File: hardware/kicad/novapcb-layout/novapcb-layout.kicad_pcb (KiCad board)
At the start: 4 copper layers, 36 x 36 mm, 70 parts, among them J1 USB-C_2.0, J10 CRSF_4P, J11 ESC_solder_pad, J12 ESC_solder_pad, J13 ESC_solder_pad, J14 ESC_solder_pad, J15 ESC_solder_pad, J16 ESC_solder_pad, J17 ESC_solder_pad, J18 ESC_solder_pad, J2 microSD_DM3AT, J3 TELEM_6P, J4 MAUCH_6P, J5 GPS_MAG_10P, J9 SWD_10P, U1 STM32H743VITx, U2 AP2112K-3.3, U3 ICM-42688-P, U4 DPS310, U5 USBLC6-2P6, Y1 8MHz

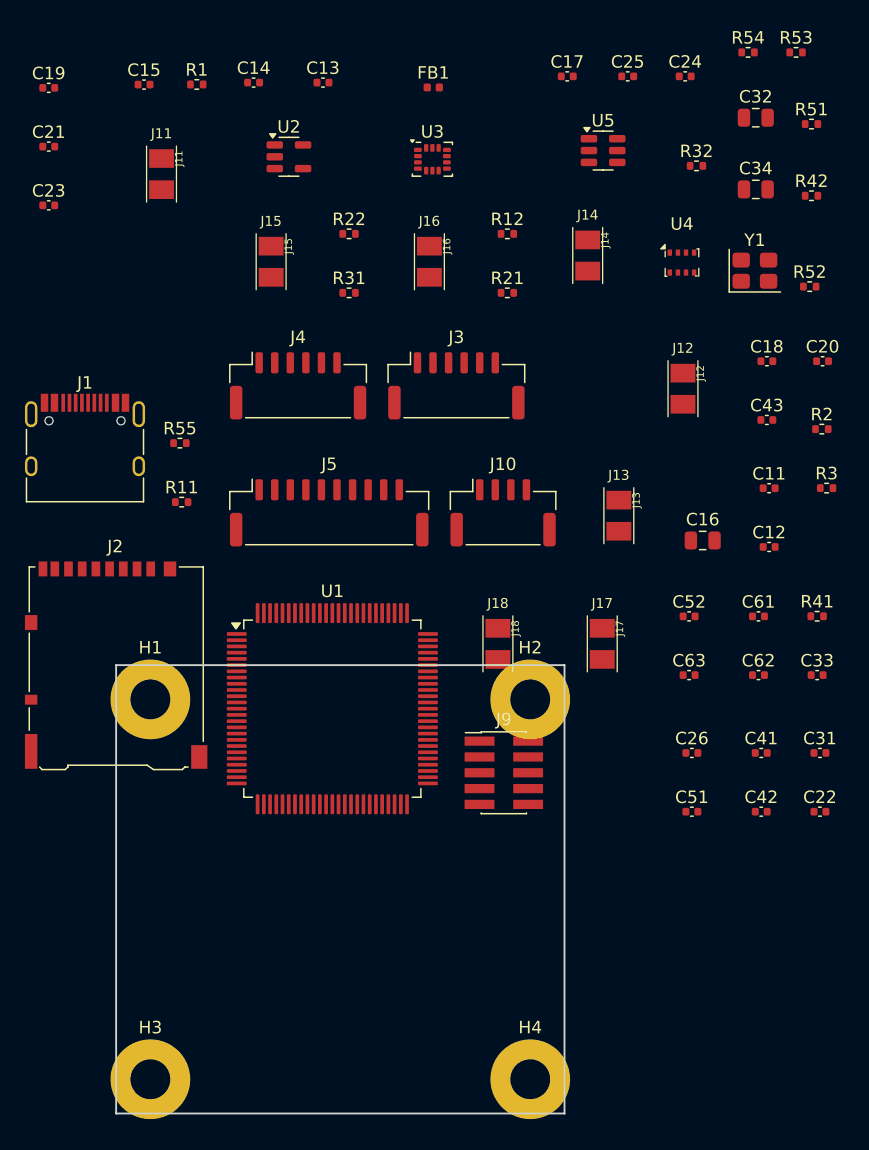
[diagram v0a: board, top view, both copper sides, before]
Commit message: Phase 4b: component placement (routing-aware first-pass) (#43)
* Phase 4b: component placement (routing-aware first-pass)

70 components placed on the 36×36 board with per-component-group
routing-aware reasoning. Master 09:00 cross-review emphasis: "4b is the
highest-leverage Phase 4 sub-phase; treat as design, not mechanics."

## Per-group placement reasoning (summary)

- MCU (U1) centered at (18,19) — geometric center for 4-edge routing
  reach; +1mm N to leave Y=0..11 for ESC pads bottom row
- Crystal (Y1) hard against MCU east (HSE pins per STM32H743V)
- LDO (U2 AP2112K) SW at (6,9) — near 5V input from Mauch path
- IMU (U3 ICM-42688-P) west of MCU at (8,22) — board-center-Y for
  rotational sensing; off-axis from LDO heat + ESC switching noise
- Baro (U4 DPS310) N of MCU at (22,28) — close to I²C2 pins
- GPS+mag (J5 JST-GH 10P) left edge
- USB-C (J1) top center — short diff pair to MCU PA11/PA12;
  USBLC6 ESD (U5) west of J1 body to clear J1 courtyard
- CRSF (J10), Telem (J3), Mauch (J4) right edge top/mid/bottom
- microSD (J2) FLIPPED TO B.CU — resolves Phase 2.5 tight-spot #1
  (microSD vs IMU vertical-clearance collision)
- 8× ESC solder pads (J11-J18) bottom edge single row, 3.0mm pitch
- SWD (J9) B.Cu under MCU center for pogo-pin programming
- 4× M3 mounting (H1-H4) corners at exact 30.5 c-to-c
- 50+ passives positioned per-IC: MCU decoupling around 4 sides ≥2.5mm
  from body edge; ADC filter near MCU PC0/PC1 (PHASE3_AUDIT §B #5);
  SDMMC pullups between J2 and MCU; CC pulldowns near J1

## Phase 2.5 sketch refinements

- J6 CAN REMOVED (phase3exit-can deliberate v1-omit) — frees right edge
- J2 microSD FLIPPED to B.Cu — resolves the IMU-vs-microSD collision
- 8× solder pads replace 2× JST-SH 4P (Phase 4a footprint swap)
- Other connectors refined for cleaner right-edge separation

## DRC honesty

`kicad-cli pcb drc --severity-error`:
- 4a baseline: 16 courtyard-overlap from kinet2pcb grid
- 4b after placement: 87 violations, 0 unconnected

Breakdown:
- 4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
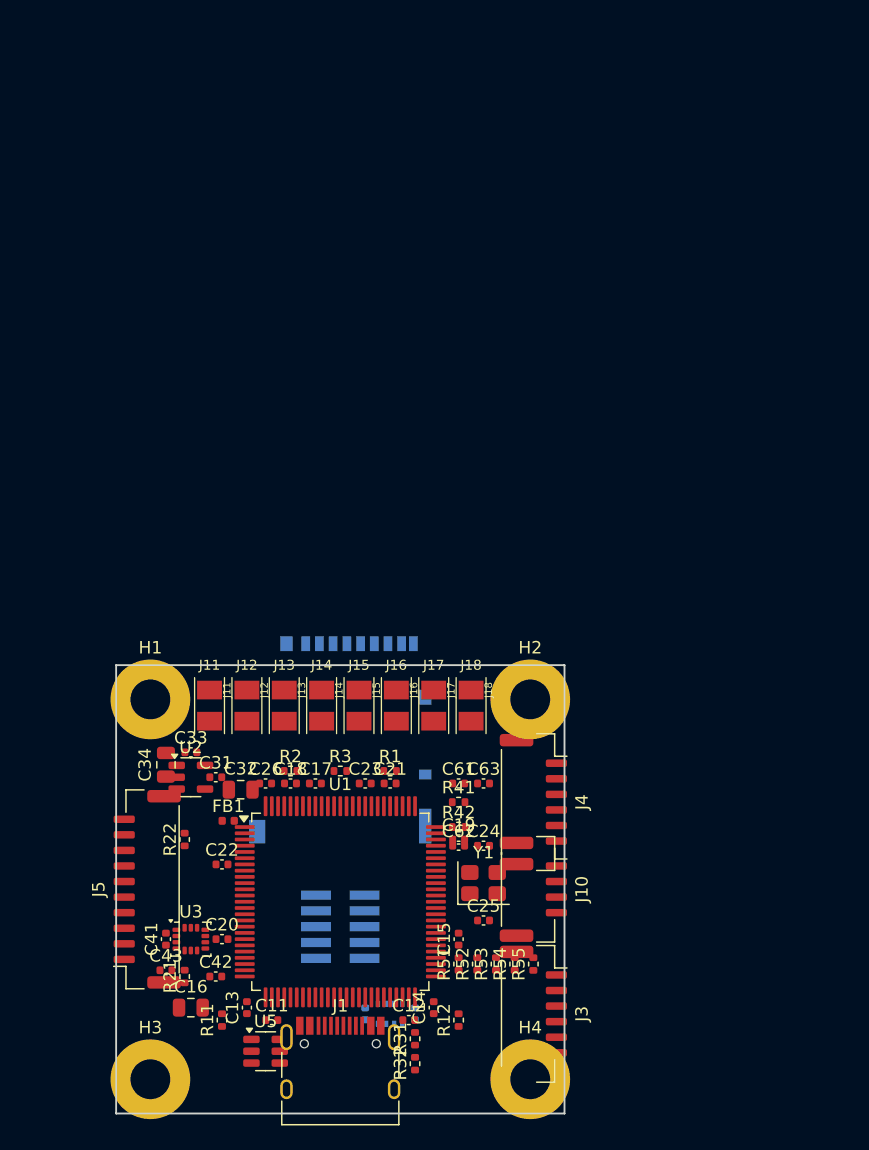
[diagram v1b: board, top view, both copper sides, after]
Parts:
- C51, C52, J2, J9, U4: moved to B.Cu
- moved U5 77.2 mm to (12.0, 31.0)
- moved R53 77.1 mm to (30.5, 24.0), turned to 90 degrees
- moved C14 75.7 mm to (25.5, 27.5), turned to 90 degrees
- moved R54 75.6 mm to (32.0, 24.0), turned to 90 degrees
- moved R32 75.5 mm to (24.0, 32.0), turned to 90 degrees
- moved C13 74.5 mm to (10.5, 27.5), turned to 90 degrees
- moved R51 73.2 mm to (27.5, 24.0), turned to 90 degrees
- moved C15 73.1 mm to (27.5, 22.0), turned to 90 degrees
- moved C25 68.8 mm to (29.5, 20.5)
- moved C19 68.7 mm to (27.5, 14.0)
- moved C32 68.0 mm to (10.0, 10.0)
- moved C20 66.9 mm to (8.50, 22.0)
- moved C34 66.2 mm to (4.00, 8.00), turned to 90 degrees
- moved U3 65.6 mm to (6.00, 22.0)
- moved C43 65.4 mm to (4.00, 24.5)
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
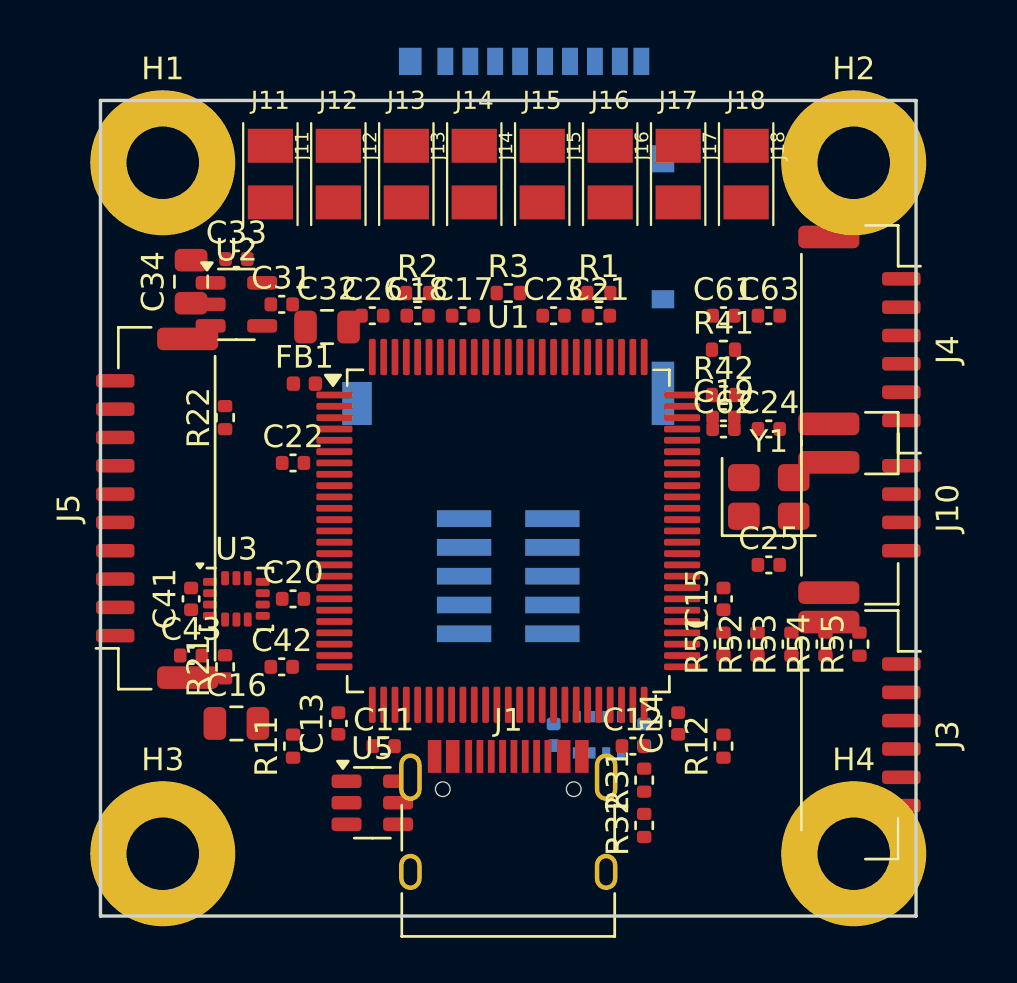
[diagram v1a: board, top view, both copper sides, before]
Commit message: Phase 4c: copper plane pour (Rule 13 stop at 4c.6 — 5 shorts persist)
Plane pour implemented per master's iter-#3 P0 pre-conditions. 4c.6
DRC re-check triggers Rule 13 stop per master's 4b adjudication
("If any do NOT resolve, that's a Rule 13 stop").

## What got done

7 copper zones added + persisted in .kicad_pcb:
- In1.Cu  GND   solid pour (full board minus 0.2mm edge inset)
- In2.Cu  +3V3  dominant (full board, low priority)
- In2.Cu  +5V   top band (Y>22): USB-C + N half of right edge
- In2.Cu  +5V   LDO strip (SW corner): U2 input
- In2.Cu  VBAT  small rect (S of MCU + J4 Mauch)
- In2.Cu  +3V3A tiny zone (MCU VDDA via FB1)
- B.Cu    GND   fill in unused areas (signal+GND-fill per fork)

DRC result:
- unconnected_items: 193 → 0 ✓ (planes connecting pads correctly)
- shorting_items: 5 → 5 (UNCHANGED — F.Cu pad-pad physical overlaps,
  plane pour on inner layers doesn't move pads)
- clearance: 13 (unchanged from 4b-rev)
- total: 18 (same as 4b-rev; planes didn't add violations but didn't
  resolve the shorts either)

## Rule 13 stop — 5 unresolved shorting_items

The 4b assumption "cap-GND shorts auto-resolve at 4c plane pour" was
WRONG. All 5 persist because they're F.Cu pad-pad physical overlaps:

1. U2 LDO pad-2 [GND] @ (4.86,9.00) ↔ C34 pad-1 [+3V3] @ (4.00,8.95)
2. U5 pad-5 [+5V] @ (13.14,31.00) ↔ J1 USB-C PTH shield [GND] @ (13.68,29.87)
3. U5 pad-6 [USB_DP] @ (13.14,30.05) ↔ J1 shield same position
4. C62 [BATT_CURRENT_SENS] @ (27.02,14.50) ↔ C19 [+3V3A] @ (27.02,14.00)
5. C26 [NRST] @ (11.52,9.50) ↔ C32 [GND] @ (10.95,10.00)

All 5 fixable by ~1-2mm targeted nudges (worker did NOT apply — 4c
scope is planes, not placement). Master adjudicates options A/B/C in
phase-4c-planes.yaml escalation_log #1; worker recommends B (4b-rev3
targeted nudges on the 5 specific F.Cu pad collisions).

## Two pcbnew Python binding bugs discovered + worked around

Both logged in KICAD9_NOTES.md (cross-machine source of truth):

1. **ZONE.SetOutline(SHAPE_POLY_SET) holds outl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
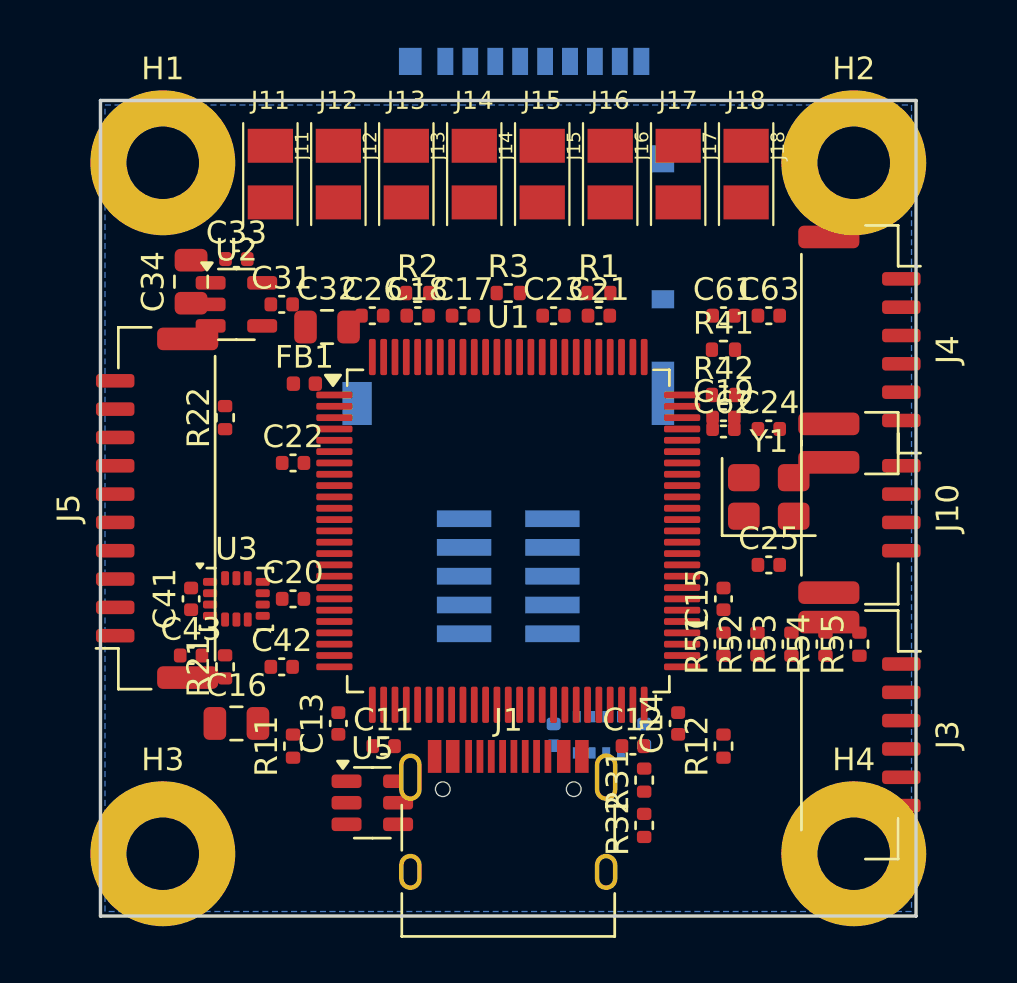
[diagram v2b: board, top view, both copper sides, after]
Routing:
- added copper zone on In2.Cu, net +3V3
- added copper zone on In2.Cu, net +3V3A
- added copper zone on In2.Cu, net +5V
- added copper zone on B.Cu, net GND
- added copper zone on In1.Cu, net GND
- added copper zone on In2.Cu, net VBAT

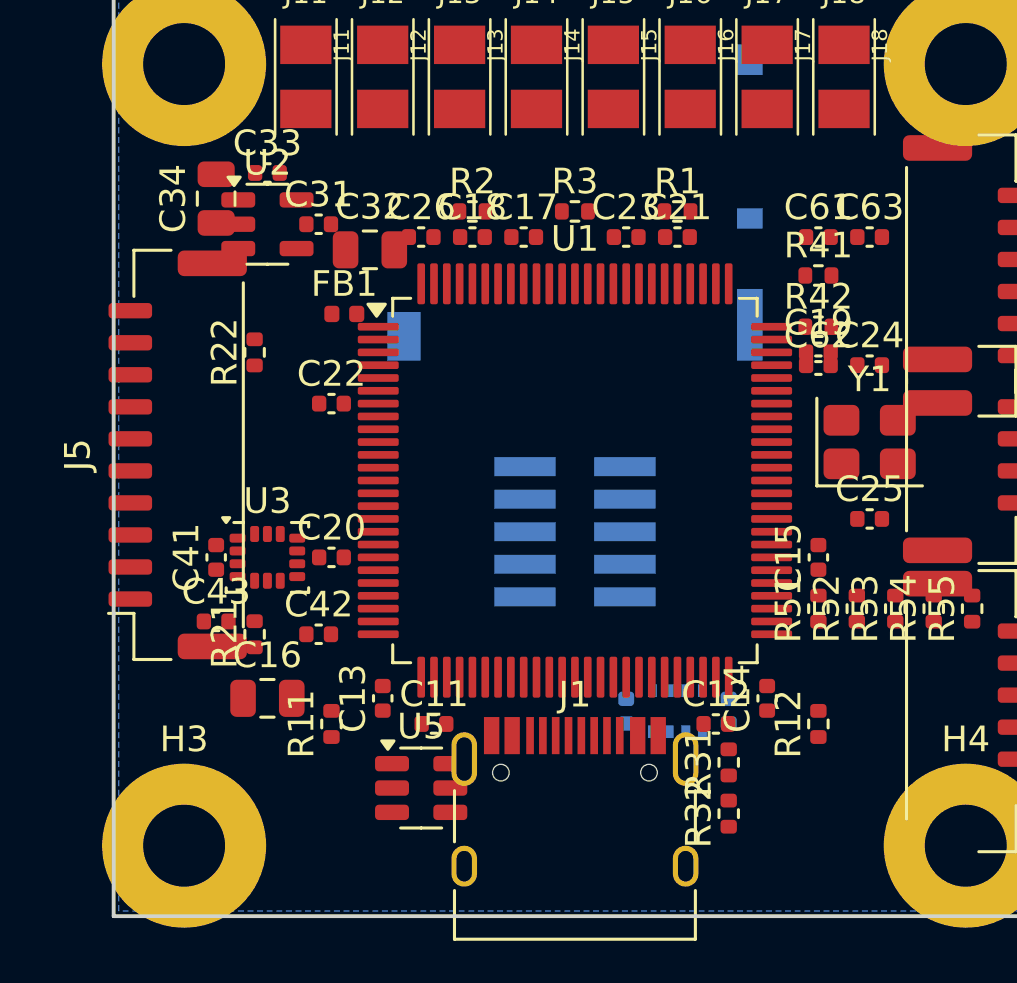
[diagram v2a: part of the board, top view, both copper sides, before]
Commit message: Phase 4c 4b-rev3: 5 targeted nudges resolve all 4c.6 shorts (5→0)
Per master 4c.6 adjudication (option B): targeted nudges on the 5 named
F.Cu pad-pad overlaps. Each by name + resolution:

1. **U2↔C34 (GND/+3V3)**: C34 was at (4,8,90°) overlapping U2 pin 2.
   First nudge (3,9) created new overlap with U2 pin 1+3 (0805 body
   1.25mm wide > expected). Final: C34 at (2.0, 9.0) — body X=1.05..2.95,
   pad-2 at X=2.95 clears U2 pin 1 (X=4.36..5.36) by 1.41mm. **RESOLVED ✓**

2+3. **U5↔J1 (+5V/GND, USB_DP/GND)**: U5 USBLC6 at (12,31), east pads
   at X=13.14 collided with J1 USB-C SW shield at X=13.68. Final: U5 at
   (10.5, 31.0) — east pads at X=11.64 clear of J1 shield by 2.04mm.
   **RESOLVED ✓** (both shorts in one nudge)

4. **C62↔C19 (BATT_CURRENT_SENS/+3V3A)**: same X-column collision at
   (27.5, 14/14.5). First nudge to (25.5, 14.5) hit MCU pin 72 SWDIO
   instead (pad X=24.88..26.48; C62 pad X=24.75..26.25 overlapped).
   Final: C62 at (24.0, 13.0) — body X=23.5..24.5 clears MCU east pad
   outer X=26.48 by 1.98mm; Y=12.5..13.5 clears MCU south pad outer
   Y=10.52 by 2mm + C19 at Y=14.0 by 0.5mm. **RESOLVED ✓**

5. **C26↔C32 (NRST/GND)**: LDO south cluster overlap. C26 kept at
   (12, 9.5) original; C32 moved 1.5mm W to (8.5, 10.0). (First-pass
   moved C26 east to (14, 9.5) but that collided with C18 already at
   (14, 9.5) — fixed by moving C32 instead.) **RESOLVED ✓**

## DRC post-4b-rev3

- shorting_items: **5 → 0 ✓** (master's mandatory verification PASSES)
- clearance: 13 (unchanged from 4b-rev — the irreducible-candidate list)
- unconnected_items: 0 (planes connect pads correctly)
- **Total: 13 violations** (was 18; reduction of 5/5 shorts)

## 13 clearance residuals (bounded list for SUPERMASTER GUI fine-tune)

Per master's 4b-rev guidance ("bounded specific list of irreducibles"):

```
J5↔R21    Power_3V3  actual=0.000mm (R21 inside J5 body envelope)
C32↔U2    Power_5V   actual=0.000mm (LDO bulk near U2 west side)
J4↔Y1     Default    actual=0.000mm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
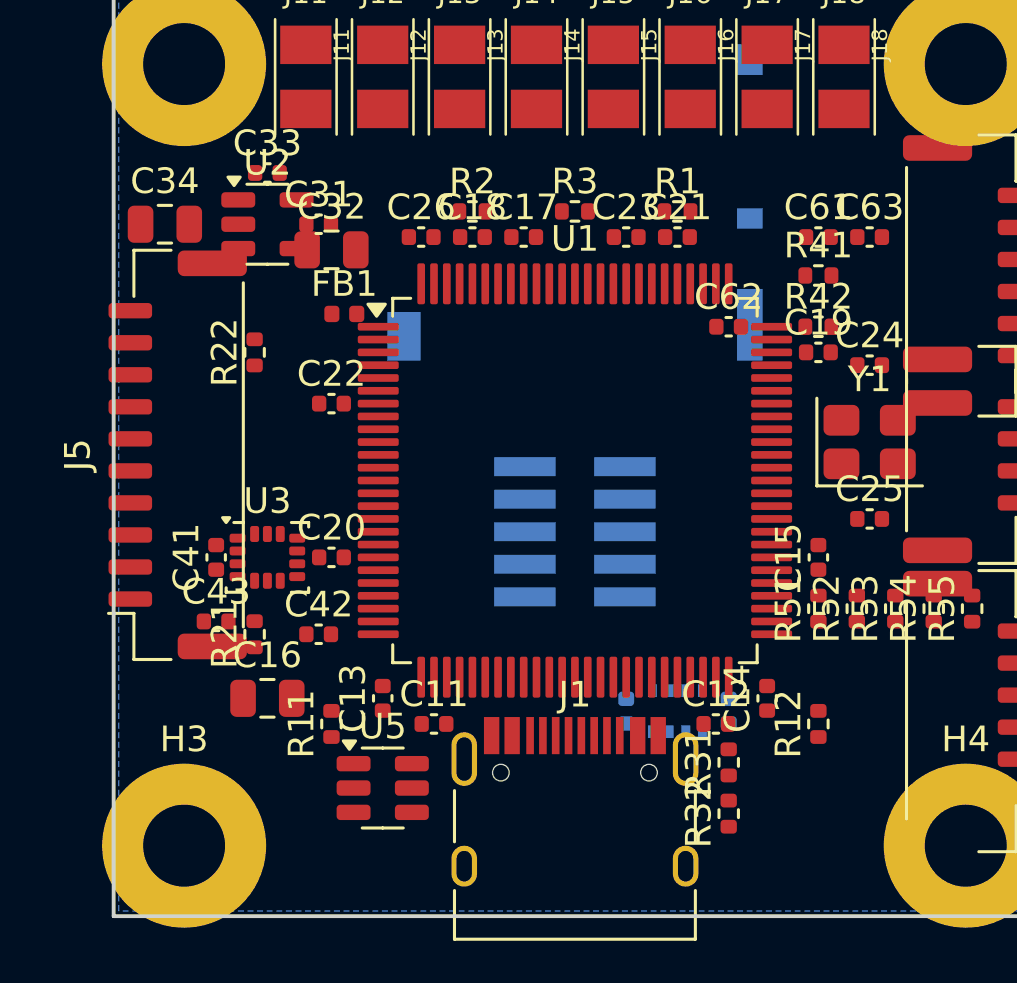
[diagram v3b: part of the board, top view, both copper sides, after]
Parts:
- moved C62 3.81 mm to (24.0, 13.0)
- moved C34 2.24 mm to (2.00, 9.00), turned to 0 degrees
- moved C32 1.50 mm to (8.50, 10.0)
- moved U5 1.50 mm to (10.5, 31.0)
